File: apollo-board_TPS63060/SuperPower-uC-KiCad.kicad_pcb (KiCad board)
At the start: 4 copper layers, 45.1 x 45.1 mm, 111 parts, among them J1 JST_PH_S2B_thru, J10 Conn_01x13_Male, J11 Conn_01x04_Male, J3 Conn_01x02_Male, J4 DNP/JST_ZH_S2B_thru, J5 DNP/JST_XH_S2B_thru, J6 Conn_01x02_Male, Q1 DMN2019UTS, Q10 2N7002A, Q11 2N7002A, Q12 DMP2035UVT, Q13 DMP2035UVT, Q14 DMP2035UVT, Q15 DMN3023L, Q2 Si3421DV, Q3 DMN3023L, Q4 2N7002A, Q5 DMP2035UVT, Q6 BSS84-7-F, Q9 2N7002A, SW1 DNP/SKRKAEE020, U1 AP9101CK6-AYTRG1, U10 TPS63060, U2 USB-C, U3 IP4220CZ6, U4 LTC4162EUFD-LAD, U5 RV-3028-C7, U8 TPS70933DRVT, U9 TPS63060

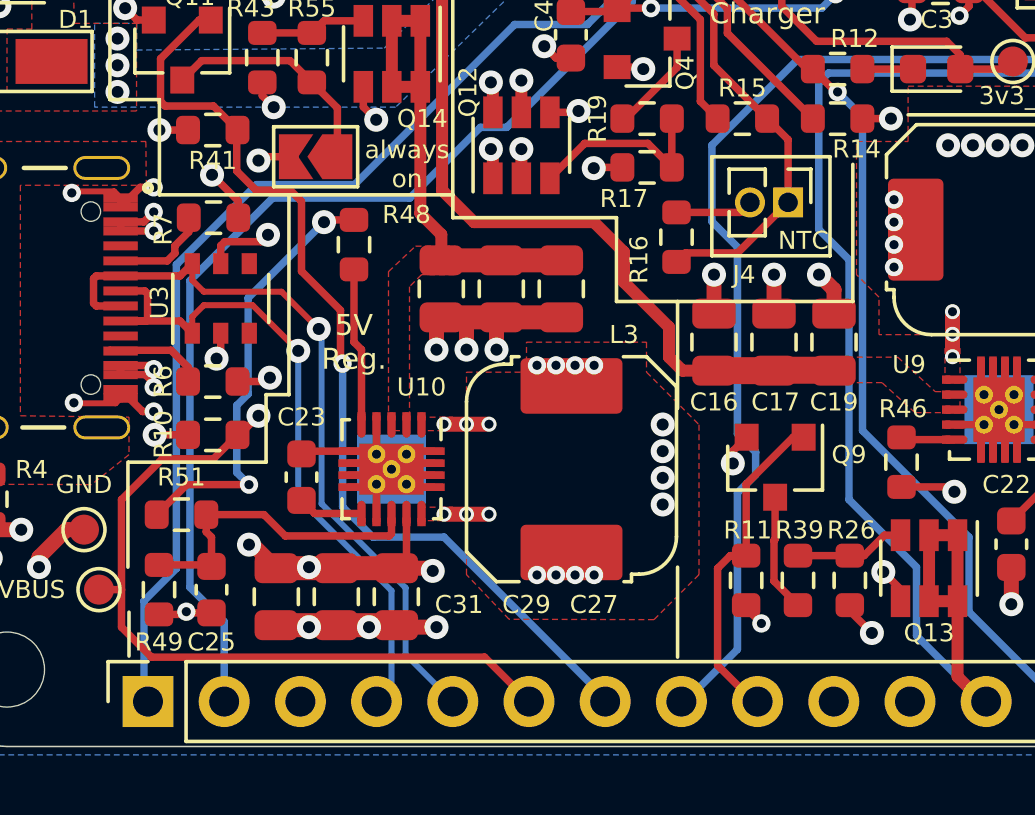
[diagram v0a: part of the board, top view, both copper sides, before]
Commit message: Update 10µF 0805 and 100nF 0603 capacitors
+ silk Ref. Des.
Rem. : Apollo Logo and name on Silkscreen Bottom seem to be lost.
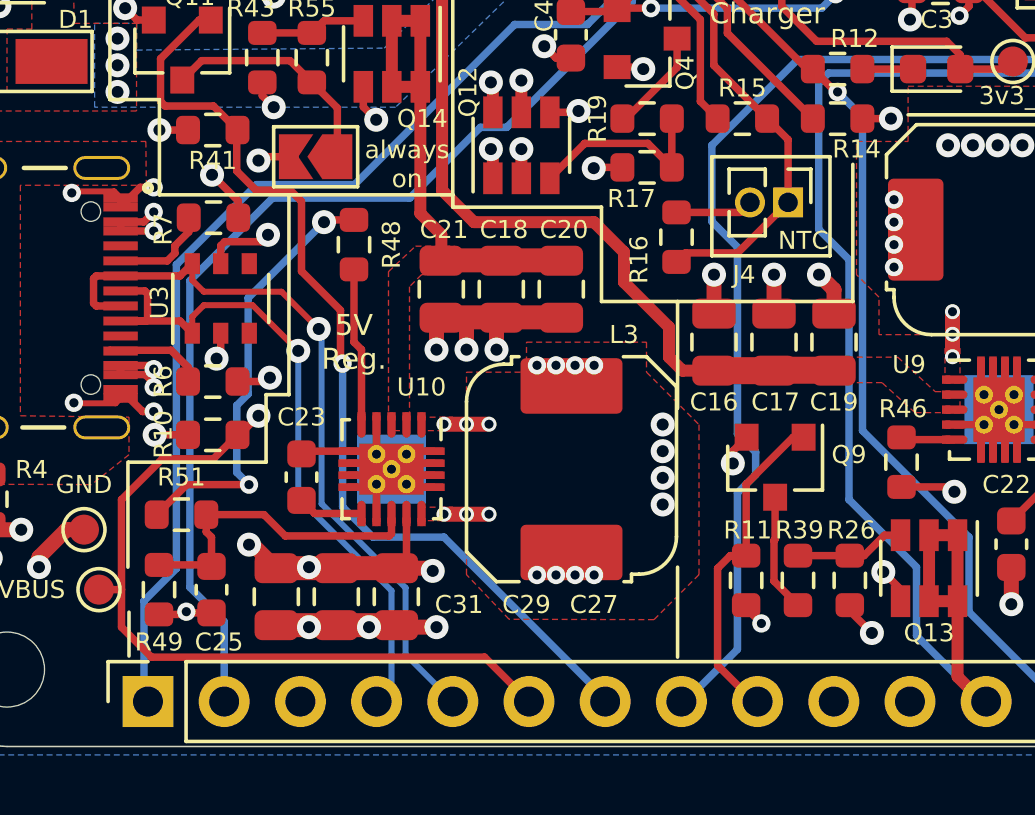
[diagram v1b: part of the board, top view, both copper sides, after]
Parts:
- C18, C20, C21: value 10μF -> CL21A106KAYNNNE
- C23: value 0.1µF -> CL10B104KB8NNNC

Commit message: Update +5V Buck-Boost Feedback resistor values
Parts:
- R49: value 130k -> 150k
- R51: value 680k -> 1.37M

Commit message: Use a new footprint for TPS63060 chips
Remove Bottom Soldermask on vias
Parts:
- U10, U9: footprint TPS63060:Texas_S-PWSON-N10_ThermalVias -> TPS63060:Texas_S-PWSON-N10_ThermalVias_NSM_vias_bottom

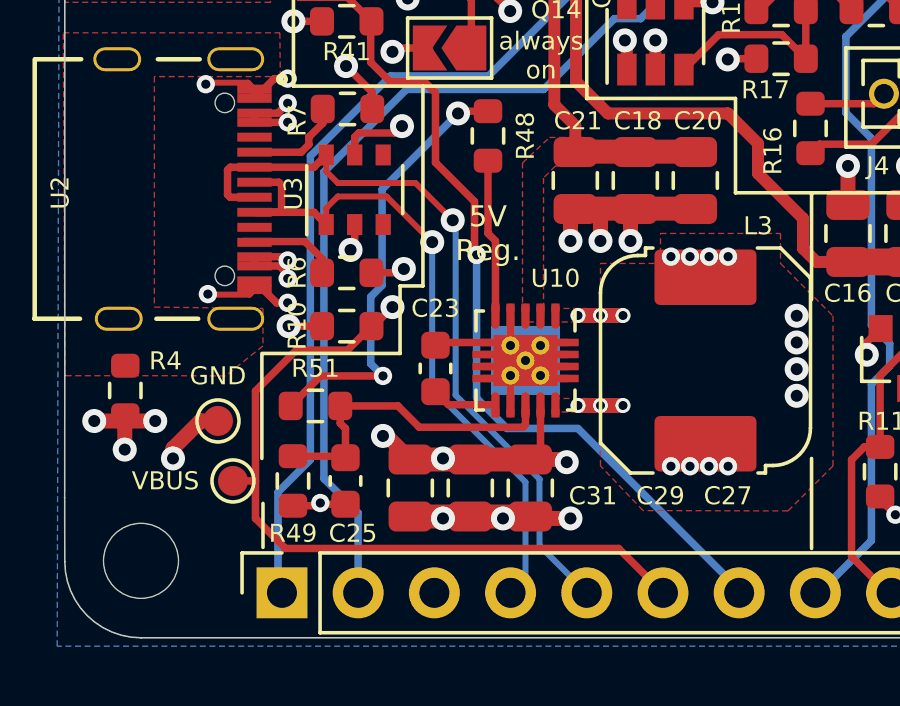
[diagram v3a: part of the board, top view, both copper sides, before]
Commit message: Improve USB Data diff. Pair length.
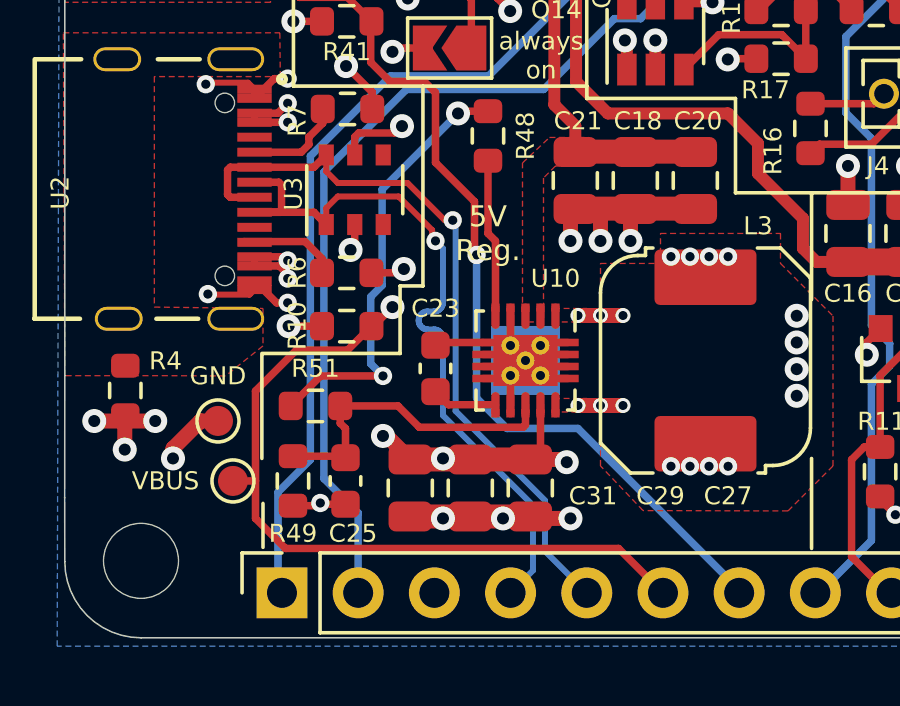
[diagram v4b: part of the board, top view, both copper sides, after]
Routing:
- net /D+: track 23.7 -> 25.4 mm

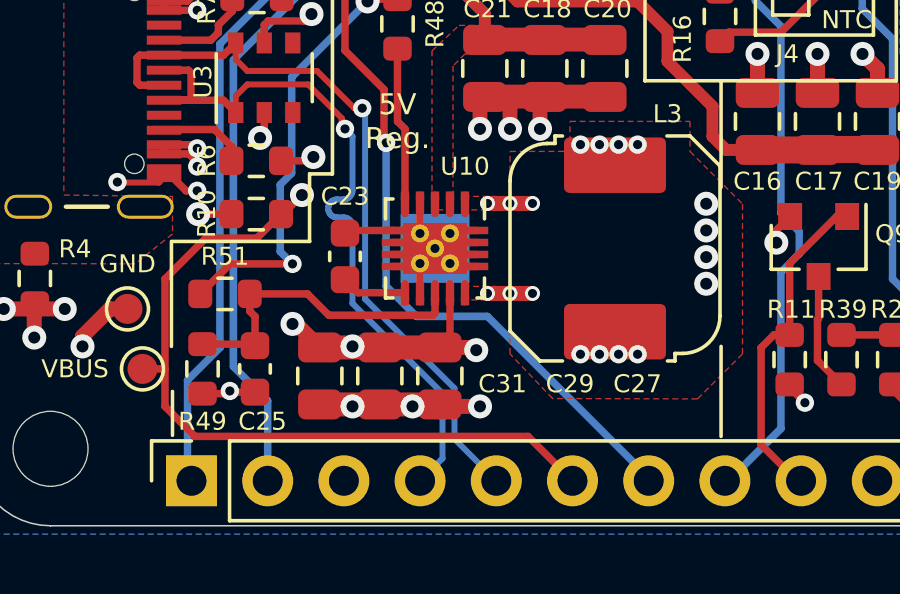
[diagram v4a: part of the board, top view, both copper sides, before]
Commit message: Update Buck-Boost Feedback Resistor values
- Use common values + bridge divider iq >3µA
- Misc. Routing : increase one track width from 0.25 to 0.28mm (+5V Output)
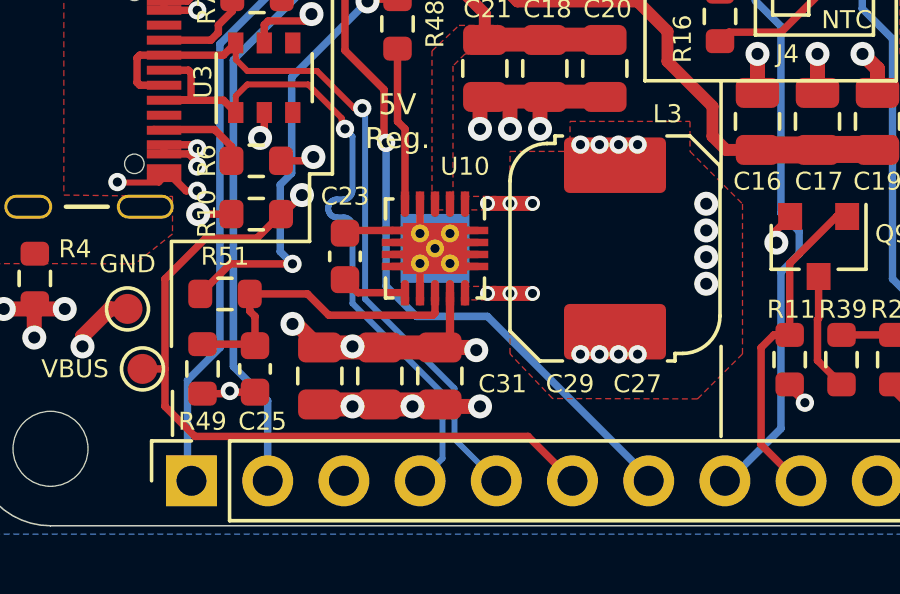
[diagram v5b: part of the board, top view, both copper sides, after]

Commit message: Update USB-C receptacle symbol fields
Add Mfr Name & ref., DataSheet + Alternative Equivalent Part
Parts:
- R47: value 150k -> 100k
- R49: value 150k -> 110k
- R50: value 845k -> 560k
- R51: value 1.37M -> 1M

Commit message: Re-Add "Apollo Logo" on Silkscreen bottom Layer
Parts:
- added G***: LOGO, logo:apollo-logo, B.Cu at (143.3, 90.6)

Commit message: Update "RTC Bypass" text position
+ Add "-A" extension pour TPS63060 variant
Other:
- board text added: "v1.00-A (2021-02)"
- board text removed: "v1.00 (2021-01)"
